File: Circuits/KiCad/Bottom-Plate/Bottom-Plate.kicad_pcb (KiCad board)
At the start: 2 copper layers, 104.1 x 104.1 mm, 8 parts

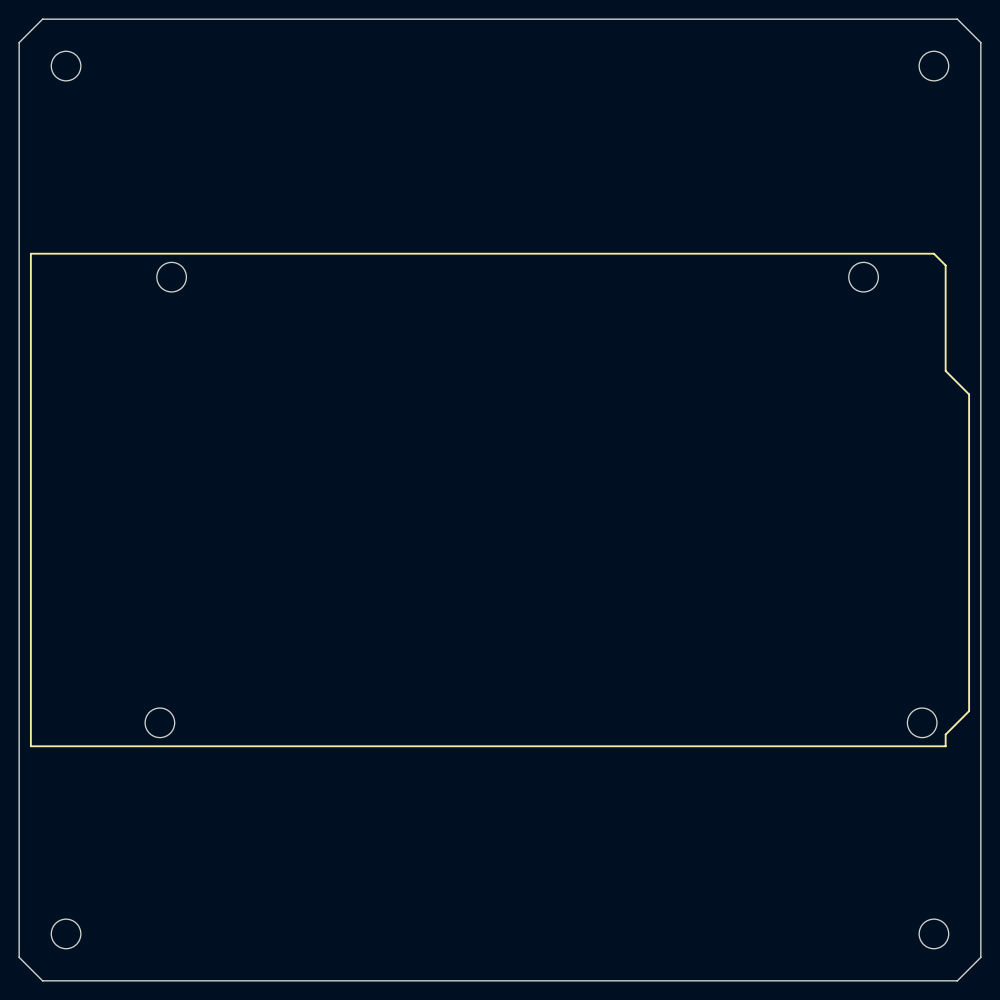
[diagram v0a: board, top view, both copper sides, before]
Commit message: Updated PCB for Bottom and Debugger (sent to manufacturer)
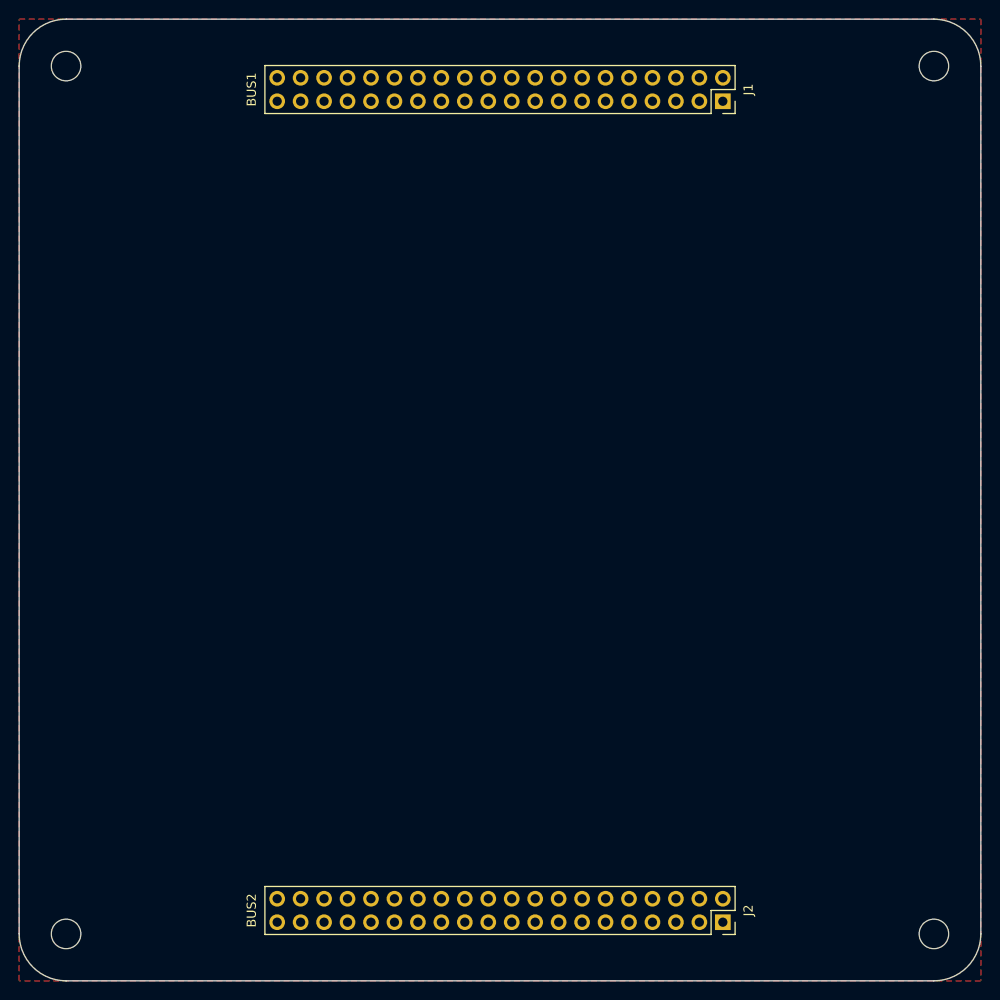
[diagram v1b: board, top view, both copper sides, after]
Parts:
- removed the H1 at (118.1, 54.6)
- removed the H1 at (124.5, 102.9)
- removed the H1 at (41.9, 102.9)
- removed the H1 at (43.2, 54.6)
- added J1: BUS1, Connector_PinSocket_2.54mm:PinSocket_2x20_P2.54mm_Vertical, F.Cu at (102.9, 35.6)
- added J2: BUS2, Connector_PinSocket_2.54mm:PinSocket_2x20_P2.54mm_Vertical, F.Cu at (102.9, 124.5)
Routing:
- added copper zone on F.Cu, net (none)
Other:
- outline, holes or cut-outs redrawn

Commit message: Documentation
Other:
- board text added: "DM-02 | Bottom Plate | Revision 1"
- board text removed: "Revision 1"
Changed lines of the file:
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@@
     (pad 1 np_thru_hole circle (at 0 0) (size 3.2 3.2) (drill 3.2) (layers *.Cu *.Mask))
+  )
+  (gr_text "DM-02 | Bottom Plate | Revision 1" (at 78.74 128.27) (layer B.SilkS)
+    (effects (font (size 1 1) (thickness 0.1)) (justify mirror))
   )
   (gr_arc (start 125.73 31.75) (end 130.81 31.75) (angle -90) (layer Edge.Cuts) (width 0.15))
@@
     (effects (font (size 3 3) (thickness 0.6)) (justify mirror))
   )
-  (gr_text "Revision 1" (at 78.74 127) (layer B.SilkS)
-    (effects (font (size 1 1) (thickness 0.1)) (justify mirror))
-  )
   (zone (net 0) (net_name "") (layer F.Cu) (hatch edge 0.508)

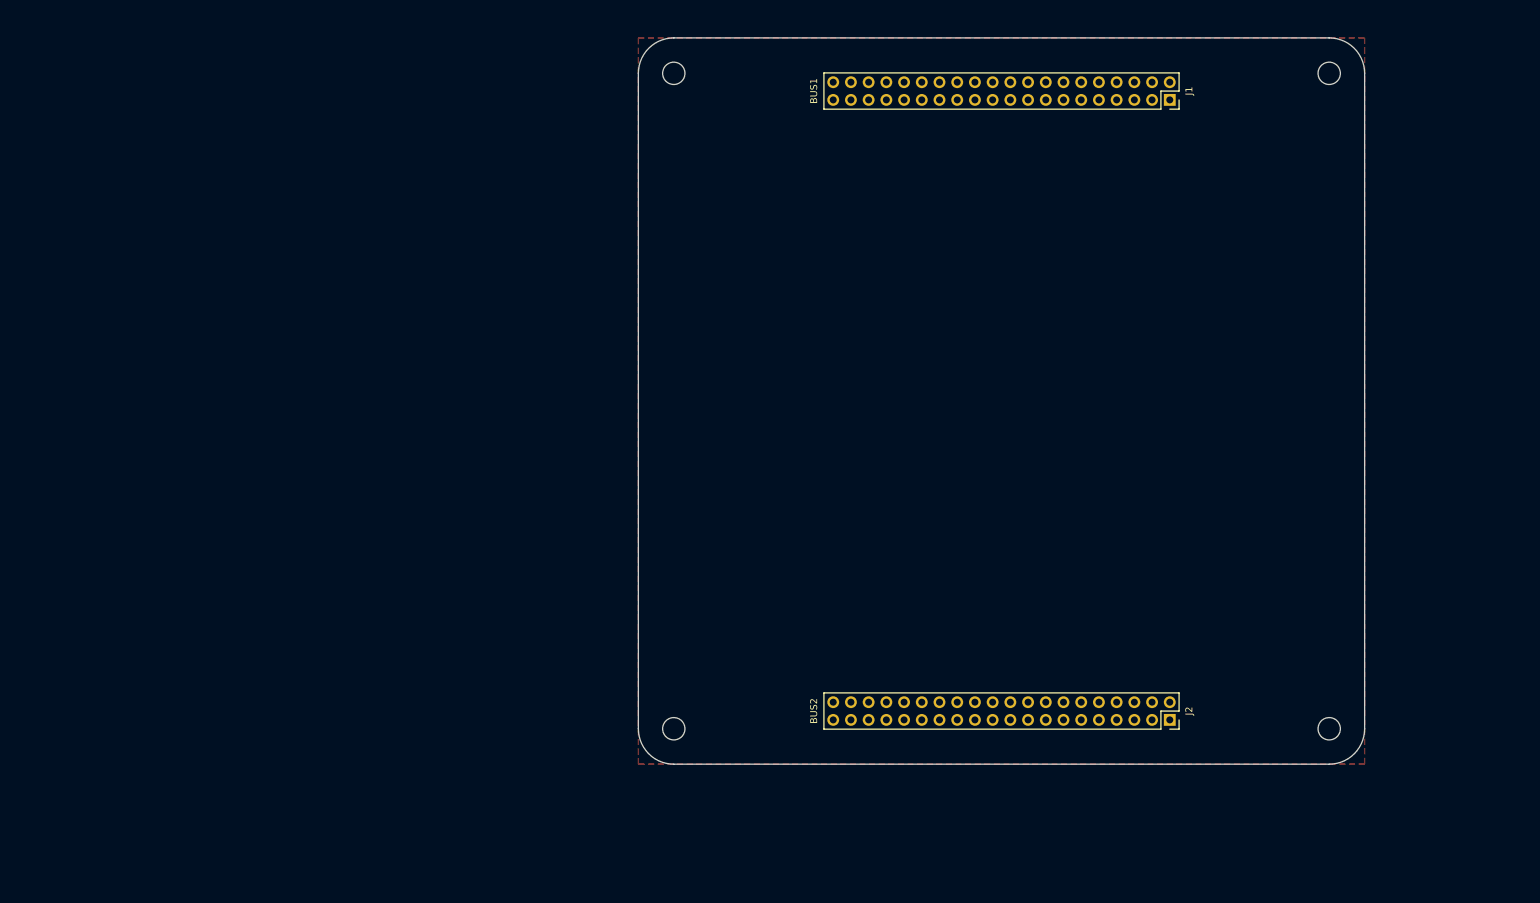
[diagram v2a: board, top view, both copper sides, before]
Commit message: Figuring out bus connections
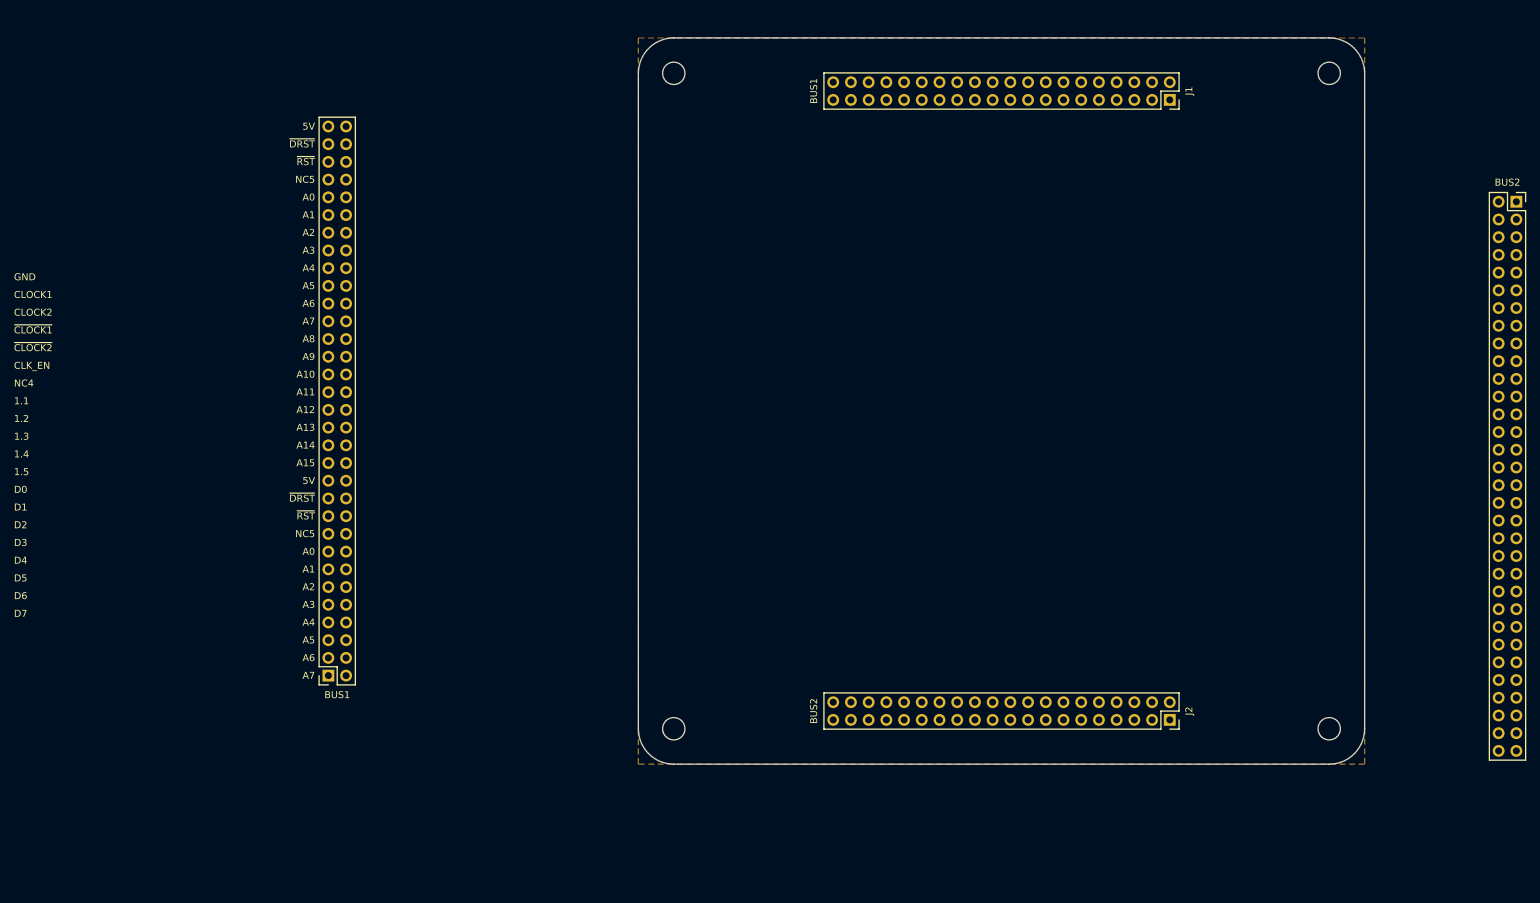
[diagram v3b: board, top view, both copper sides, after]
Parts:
- added BUS1: Conn_02x32_Odd_Even, Connector_PinSocket_2.54mm:PinSocket_2x32_P2.54mm_Vertical, F.Cu at (-17.8, 118.1)
- added BUS2: Conn_02x32_Odd_Even, Connector_PinSocket_2.54mm:PinSocket_2x32_P2.54mm_Vertical, F.Cu at (152.6, 50.2)
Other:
- board text added: "1.1"
- board text added: "1.2"
- board text added: "1.3"
- board text added: "1.4"
- board text added: "1.5"
- board text added: "5V"
- board text added: "A0"
- board text added: "A1"
- board text added: "A10"
- board text added: "A11"
- board text added: "A12"
- board text added: "A13"
- board text added: "A14"
- board text added: "A15"
- board text added: "A2"
- board text added: "A3"
- board text added: "A4"
- board text added: "A5"
- board text added: "A6"
- board text added: "A7"
- board text added: "A8"
- board text added: "A9"
- board text added: "CLK_EN"
- board text added: "CLOCK1"
- board text added: "CLOCK2"
- board text added: "D0"
- board text added: "D1"
- board text added: "D2"
- board text added: "D3"
- board text added: "D4"
- board text added: "D5"
- board text added: "D6"
- board text added: "D7"
- board text added: "DM-02 | Bottom Plate | Revision 2"
- board text added: "GND"
- board text added: "NC4"
- board text added: "NC5"
- board text added: "~CLOCK1"
- board text added: "~CLOCK2"
- board text added: "~DRST"
- board text added: "~RST"
- board text removed: "DM-02 | Bottom Plate | Revision 1"

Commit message: Updated bus connections and bottom plate design
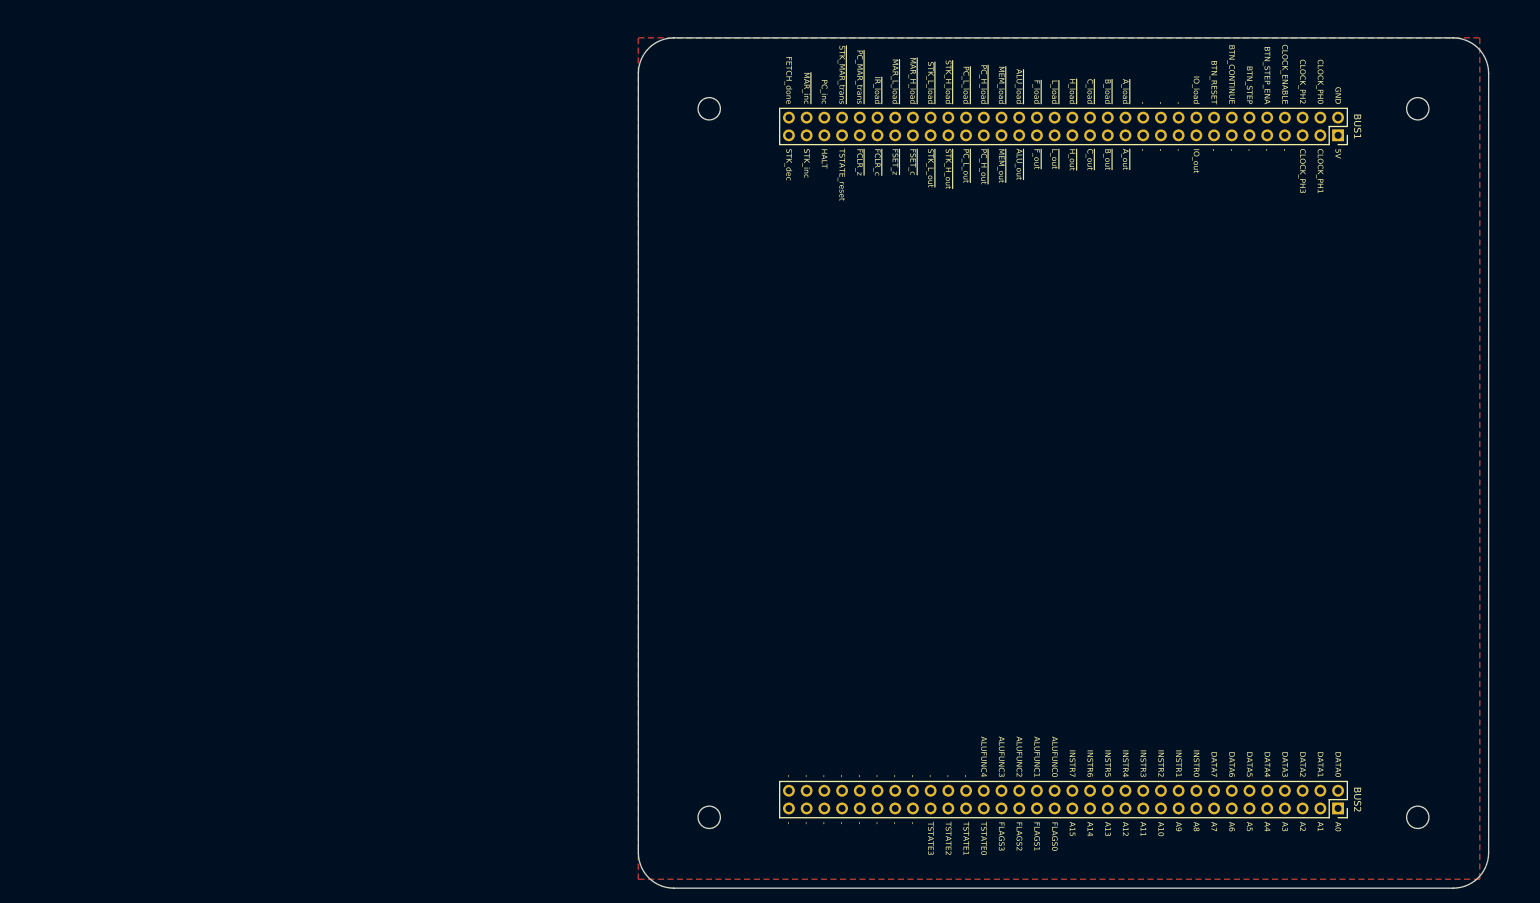
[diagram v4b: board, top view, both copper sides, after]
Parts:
- removed J1: BUS1, Connector_PinSocket_2.54mm:PinSocket_2x20_P2.54mm_Vertical
- removed J2: BUS2, Connector_PinSocket_2.54mm:PinSocket_2x20_P2.54mm_Vertical
- moved BUS1 164.2 mm to (127.0, 40.6), turned to 270 degrees
- moved BUS2 90.7 mm to (127.0, 137.2), turned to 270 degrees
- moved H3 18.0 mm to (138.4, 138.4)
- moved H2 13.7 mm to (36.8, 138.4)
- moved H4 13.7 mm to (138.4, 36.8)
- moved H1 7.18 mm to (36.8, 36.8)
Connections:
- net /ALU_load renamed /~ALU_out
- net /ALU_out renamed /~ALU_load
- net /A_load renamed /~A_out
- net /A_out renamed /~A_load
- net /B_load renamed /~B_out
- net /B_out renamed /~B_load
- net /C_load renamed /~C_out
- net /C_out renamed /~C_load
- net /FCLR_c renamed /~IR_load
- net /FCLR_z renamed /~PC_MAR_transfer
- net /FSET_c renamed /~MAR_H_load
- net /FSET_z renamed /~MAR_L_load
- net /F_load renamed /~F_out
- net /F_out renamed /~F_load
- net /H_load renamed /~H_out
- net /H_out renamed /~H_load
- net /IR_load renamed /~FCLR_c
- net /L_load renamed /~L_out
- net /L_out renamed /~L_load
- net /MAR_H_load renamed /~FSET_c
- net /MAR_L_load renamed /~FSET_z
- net /MEM_load renamed /~MEM_out
- net /MEM_out renamed /~MEM_load
- net /PC_H_load renamed /~PC_H_out
- net /PC_H_out renamed /~PC_H_load
- net /PC_L_load renamed /~PC_L_out
- net /PC_L_out renamed /~PC_L_load
- net /PC_MAR_transfer renamed /~FCLR_z
- net /STK_H_load renamed /~STK_H_out
- net /STK_H_out renamed /~STK_H_load
- net /STK_L_load renamed /~STK_L_out
- net /STK_L_out renamed /~STK_L_load
- BUS1 pad 1: /GND -> /5V
- BUS1 pad 10: Net-(BUS1-Pad10) -> /BTN_STEP_ENABLE
- BUS1 pad 11: /BTN_STEP -> Net-(BUS1-Pad11)
- BUS1 pad 12: Net-(BUS1-Pad12) -> /BTN_STEP
- BUS1 pad 13: /BTN_CONTINUE -> Net-(BUS1-Pad13)
- BUS1 pad 14: Net-(BUS1-Pad14) -> /BTN_CONTINUE
- BUS1 pad 15: /BTN_RESET -> Net-(BUS1-Pad15)
- BUS1 pad 16: Net-(BUS1-Pad16) -> /BTN_RESET
- BUS1 pad 17: /IO_load -> /IO_out
- BUS1 pad 18: /IO_out -> /IO_load
- BUS1 pad 2: /5V -> /GND
- BUS1 pad 3: /CLOCK_PH0 -> /CLOCK_PH1
- BUS1 pad 4: /CLOCK_PH1 -> /CLOCK_PH0
- BUS1 pad 5: /CLOCK_PH2 -> /CLOCK_PH3
- BUS1 pad 57: /STK_MAR_transfer -> /TSTATE_reset
- BUS1 pad 58: /TSTATE_reset -> /~STK_MAR_transfer
- BUS1 pad 59: /PC_inc -> /HALT
- BUS1 pad 6: /CLOCK_PH3 -> /CLOCK_PH2
- BUS1 pad 60: /HALT -> /PC_inc
- BUS1 pad 61: /MAR_inc -> /STK_inc
- BUS1 pad 62: /STK_inc -> /~MAR_inc
- BUS1 pad 63: /FETCH_done -> /STK_dec
- BUS1 pad 64: /STK_dec -> /FETCH_done
- BUS1 pad 7: /CLOCK_ENABLE -> Net-(BUS1-Pad7)
- BUS1 pad 8: Net-(BUS1-Pad8) -> /CLOCK_ENABLE
- BUS1 pad 9: /BTN_STEP_ENABLE -> Net-(BUS1-Pad9)
- BUS2 pad 1: /DATA0 -> /A0
- BUS2 pad 10: /A4 -> /DATA4
- BUS2 pad 11: /DATA5 -> /A5
- BUS2 pad 12: /A5 -> /DATA5
- BUS2 pad 13: /DATA6 -> /A6
- BUS2 pad 14: /A6 -> /DATA6
- BUS2 pad 15: /DATA7 -> /A7
- BUS2 pad 16: /A7 -> /DATA7
- BUS2 pad 17: /INSTR0 -> /A8
- BUS2 pad 18: /A8 -> /INSTR0
- BUS2 pad 19: /INSTR1 -> /A9
- BUS2 pad 2: /A0 -> /DATA0
- BUS2 pad 20: /A9 -> /INSTR1
- BUS2 pad 21: /INSTR2 -> /A10
- BUS2 pad 22: /A10 -> /INSTR2
- BUS2 pad 23: /INSTR3 -> /A11
- BUS2 pad 24: /A11 -> /INSTR3
- BUS2 pad 25: /INSTR4 -> /A12
- BUS2 pad 26: /A12 -> /INSTR4
- BUS2 pad 27: /INSTR5 -> /A13
- BUS2 pad 28: /A13 -> /INSTR5
- BUS2 pad 29: /INSTR6 -> /A14
- BUS2 pad 3: /DATA1 -> /A1
- BUS2 pad 30: /A14 -> /INSTR6
- BUS2 pad 31: /INSTR7 -> /A15
- BUS2 pad 32: /A15 -> /INSTR7
- BUS2 pad 33: /ALUFUNC0 -> /FLAGS0
- BUS2 pad 34: /FLAGS0 -> /ALUFUNC0
- BUS2 pad 35: /ALUFUNC1 -> /FLAGS1
- BUS2 pad 36: /FLAGS1 -> /ALUFUNC1
- BUS2 pad 37: /ALUFUNC2 -> /FLAGS2
- BUS2 pad 38: /FLAGS2 -> /ALUFUNC2
- BUS2 pad 39: /ALUFUNC3 -> /FLAGS3
- BUS2 pad 4: /A1 -> /DATA1
- BUS2 pad 40: /FLAGS3 -> /ALUFUNC3
- BUS2 pad 41: /ALUFUNC4 -> /TSTATE0
- BUS2 pad 42: /TSTATE0 -> /ALUFUNC4
- BUS2 pad 43: Net-(BUS2-Pad43) -> /TSTATE1
- BUS2 pad 44: /TSTATE1 -> Net-(BUS2-Pad44)
- BUS2 pad 45: Net-(BUS2-Pad45) -> /TSTATE2
- BUS2 pad 46: /TSTATE2 -> Net-(BUS2-Pad46)
- BUS2 pad 47: Net-(BUS2-Pad47) -> /TSTATE3
- BUS2 pad 48: /TSTATE3 -> Net-(BUS2-Pad48)
- BUS2 pad 5: /DATA2 -> /A2
- BUS2 pad 6: /A2 -> /DATA2
- BUS2 pad 7: /DATA3 -> /A3
- BUS2 pad 8: /A3 -> /DATA3
- BUS2 pad 9: /DATA4 -> /A4
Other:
- board size 104.1 x 104.1 mm -> 121.9 x 121.9 mm
- board text added: "-"
- board text added: "ALUFUNC0"
- board text added: "ALUFUNC1"
- board text added: "ALUFUNC2"
- board text added: "ALUFUNC3"
- board text added: "ALUFUNC4"
- board text added: "BTN_CONTINUE"
- board text added: "BTN_RESET"
- board text added: "BTN_STEP"
- board text added: "BTN_STEP_ENA"
- board text added: "CLOCK_ENABLE"
- board text added: "CLOCK_PH0"
- board text added: "CLOCK_PH1"
- board text added: "CLOCK_PH2"
- board text added: "CLOCK_PH3"
- board text added: "DATA0"
- board text added: "DATA1"
- board text added: "DATA2"
- board text added: "DATA3"
- board text added: "DATA4"
- board text added: "DATA5"
- board text added: "DATA6"
- board text added: "DATA7"
- board text added: "FETCH_done"
- board text added: "FLAGS0"
- board text added: "FLAGS1"
- board text added: "FLAGS2"
- board text added: "FLAGS3"
- board text added: "HALT"
- board text added: "INSTR0"
- board text added: "INSTR1"
- board text added: "INSTR2"
- board text added: "INSTR3"
- board text added: "INSTR4"
- board text added: "INSTR5"
- board text added: "INSTR6"
- board text added: "INSTR7"
- board text added: "IO_load"
- board text added: "IO_out"
- board text added: "PC_inc"
- board text added: "STK_dec"
- board text added: "STK_inc"
- board text added: "TSTATE0"
- board text added: "TSTATE1"
- board text added: "TSTATE2"
- board text added: "TSTATE3"
- board text added: "TSTATE_reset"
- board text added: "https://dutchmaker.com"
- board text added: "~ALU_load"
- board text added: "~ALU_out"
- board text added: "~A_load"
- board text added: "~A_out"
- board text added: "~B_load"
- board text added: "~B_out"
- board text added: "~C_load"
- board text added: "~C_out"
- board text added: "~FCLR_c"
- board text added: "~FCLR_z"
- board text added: "~FSET_c"
- board text added: "~FSET_z"
- board text added: "~F_load"
- board text added: "~F_out"
- board text added: "~H_load"
- board text added: "~H_out"
- board text added: "~IR_load"
- board text added: "~L_load"
- board text added: "~L_out"
- board text added: "~MAR_H_load"
- board text added: "~MAR_L_load"
- board text added: "~MAR_inc"
- board text added: "~MEM_load"
- board text added: "~MEM_out"
- board text added: "~PC_H_load"
- board text added: "~PC_H_out"
- board text added: "~PC_L_load"
- board text added: "~PC_L_out"
- board text added: "~PC_MAR_trans"
- board text added: "~STK_H_load"
- board text added: "~STK_H_out"
- board text added: "~STK_L_load"
- board text added: "~STK_L_out"
- board text added: "~STK_MAR_trans"
- board text removed: "1.1"
- board text removed: "1.2"
- board text removed: "1.3"
- board text removed: "1.4"
- board text removed: "1.5"
- board text removed: "CLK_EN"
- board text removed: "CLOCK1"
- board text removed: "CLOCK2"
- board text removed: "D0"
- board text removed: "D1"
- board text removed: "D2"
- board text removed: "D3"
- board text removed: "D4"
- board text removed: "D5"
- board text removed: "D6"
- board text removed: "D7"
- board text removed: "NC4"
- board text removed: "NC5"
- board text removed: "https://github.com/DutchMaker/DM-02"
- board text removed: "~CLOCK1"
- board text removed: "~CLOCK2"
- board text removed: "~DRST"
- board text removed: "~RST"
